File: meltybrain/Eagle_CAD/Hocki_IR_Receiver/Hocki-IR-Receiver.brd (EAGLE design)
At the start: 42 x 34 mm, 68 parts, among them J1 SM03B-SRSS-TB(LF)(SN), U1 OPA2380AIDGKR, U10 LMH6612MAX/NOPB, U11 LMH6612MAX/NOPB, U2 OPA2380AIDGKR, U3 TLV3502AIDCNR, U4 TLV3502AIDCNR, U5 SN74LVC1G58DCKR, U6 NL27WZ32USG, U7 TMUX1204DGSR, U8 AP2210K-5.0TRG1, U9 TLV73310PDBVT

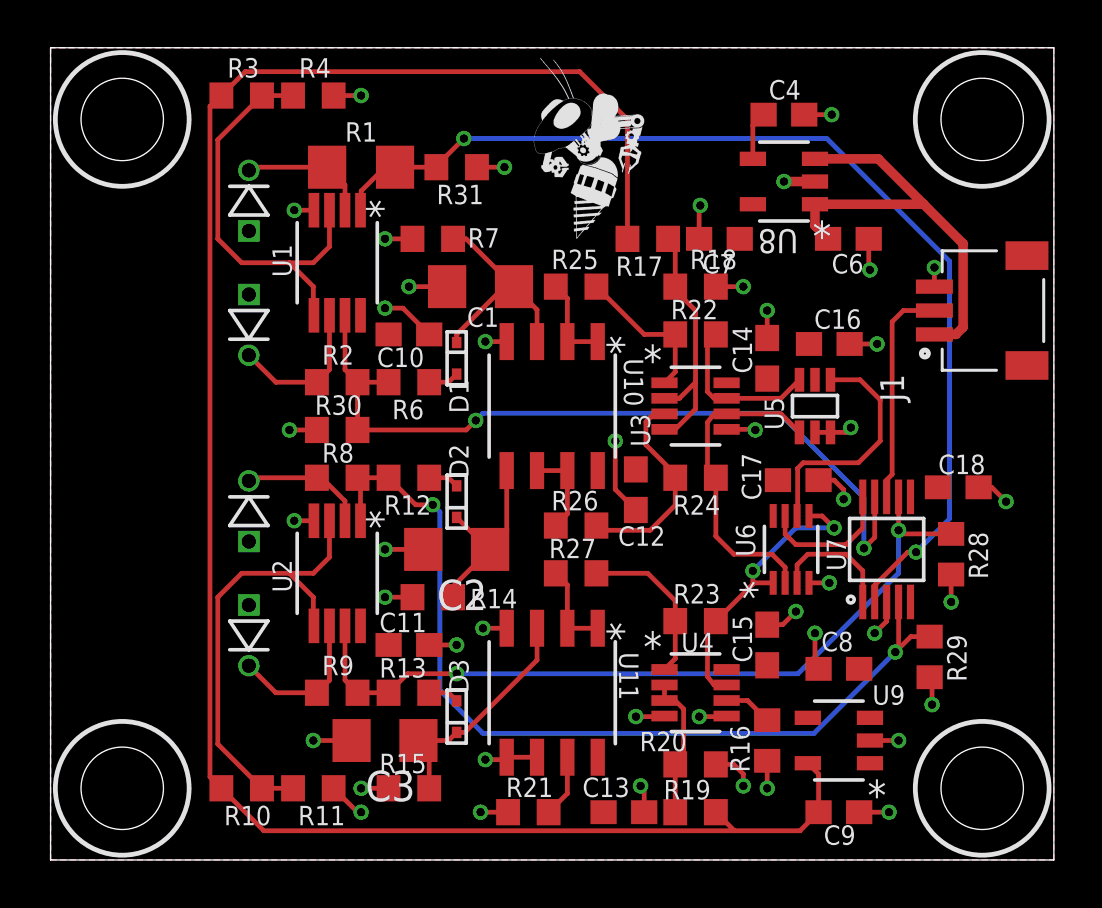
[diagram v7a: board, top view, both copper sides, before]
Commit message: power in
traces under capacitors be sketch...tried to avoid...
24-9 regulator is in
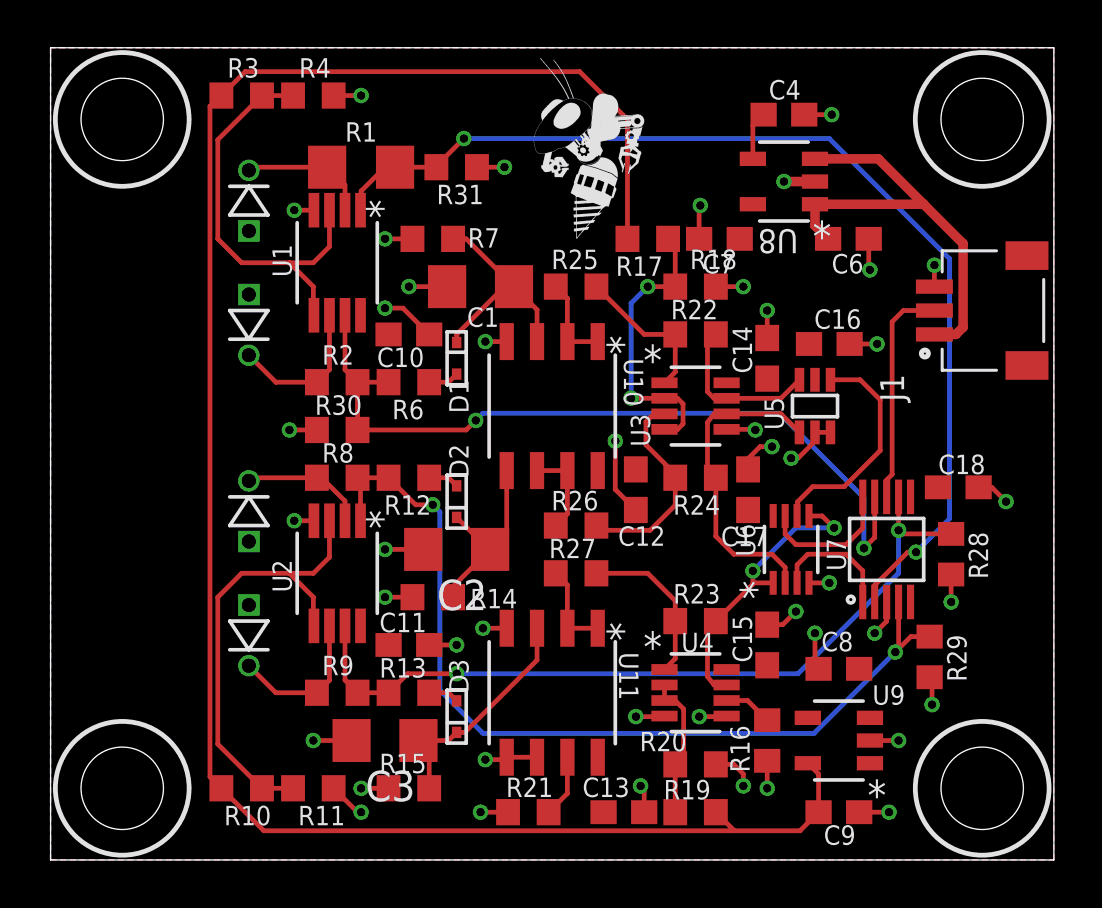
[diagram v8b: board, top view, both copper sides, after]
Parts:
- moved C17 2.14 mm to (29.2, 15.5), turned to 90 degrees
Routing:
- net N$13: track 10.8 -> 12.2 mm, vias 0 -> 2
- net GND: track 58.7 -> 59.6 mm
- net N$9: track 10.1 -> 9.50 mm
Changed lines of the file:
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@@
 <drawing>
 <settings>
-<setting alwaysvectorfont="no"/>
+<setting alwaysvectorfont="yes"/>
 <setting verticaltext="up"/>
 </settings>
@@
 <attribute name="VALUE" x="31.965" y="19.695" size="1.27" layer="27"/>
 </element>
-<element name="C17" library="rcl" library_urn="urn:adsk.eagle:library:334" package="C0603" package3d_urn="urn:adsk.eagle:package:23616/2" value="0.1u" x="31.3" y="15.9" smashed="yes">
-<attribute name="NAME" x="28.935" y="17.035" size="0.8128" layer="25" rot="R270"/>
-<attribute name="POPULARITY" value="37" x="31.3" y="15.9" size="1.778" layer="27" display="off"/>
-<attribute name="SPICEPREFIX" value="C" x="31.3" y="15.9" size="1.778" layer="27" display="off"/>
-<attribute name="VALUE" x="30.665" y="13.995" size="1.27" layer="27"/>
+<element name="C17" library="rcl" library_urn="urn:adsk.eagle:library:334" package="C0603" package3d_urn="urn:adsk.eagle:package:23616/2" value="0.1u" x="29.2" y="15.5" smashed="yes" rot="R90">
+<attribute name="NAME" x="28.065" y="13.135" size="0.8128" layer="25"/>
+<attribute name="POPULARITY" value="37" x="29.2" y="15.5" size="1.778" layer="27" rot="R90" display="off"/>
+<attribute name="SPICEPREFIX" value="C" x="29.2" y="15.5" size="1.778" layer="27" rot="R90" display="off"/>
+<attribute name="VALUE" x="31.105" y="14.865" size="1.27" layer="27" rot="R90"/>
 </element>
 <element name="C18" library="rcl" library_urn="urn:adsk.eagle:library:334" package="C0603" package3d_urn="urn:adsk.eagle:package:23616/2" value="0.1u" x="38" y="15.6" smashed="yes">
@@
 <wire x1="30" y1="4.15" x2="30" y2="3" width="0.2" layer="1"/>
 <via x="30" y="3" extent="1-16" drill="0.35"/>
-<wire x1="32" y1="17.9" x2="32.003790625" y2="17.896209375" width="0.2" layer="1"/>
-<wire x1="32.65" y1="17.9" x2="32.00758125" y2="17.9" width="0.2" layer="1"/>
-<wire x1="32.00758125" y1="17.9" x2="32.003790625" y2="17.896209375" width="0.2" layer="1"/>
 <wire x1="29" y1="3.1" x2="29" y2="3.6" width="0.2" layer="1"/>
 <wire x1="29" y1="3.6" x2="28.6" y2="4" width="0.2" layer="1"/>
@@
 <wire x1="34.6" y1="21.6" x2="33.45" y2="21.6" width="0.2" layer="1"/>
 <via x="34.6" y="21.6" extent="1-16" drill="0.35"/>
-<via x="33.2" y="15.1" extent="1-16" drill="0.35"/>
-<wire x1="32.15" y1="15.9" x2="32.8" y2="15.9" width="0.2" layer="1"/>
-<wire x1="33.2" y1="15.5" x2="33.2" y2="15.1" width="0.2" layer="1"/>
-<wire x1="33.2" y1="15.5" x2="32.8" y2="15.9" width="0.2" layer="1"/>
-<wire x1="32.65" y1="17.9" x2="33.3" y2="17.9" width="0.2" layer="1"/>
-<wire x1="33.3" y1="17.9" x2="33.5" y2="18.1" width="0.2" layer="1"/>
-<via x="33.5" y="18.1" extent="1-16" drill="0.35"/>
 <wire x1="35" y1="10.8" x2="35" y2="9.9936" width="0.2" layer="1"/>
 <wire x1="35" y1="9.9936" x2="34.5" y2="9.4936" width="0.2" layer="1"/>
@@
 <via x="30.7" y="28.4" extent="1-16" drill="0.35"/>
 <contactref element="J1" pad="3"/>
-<wire x1="37" y1="24" x2="37" y2="24.8" width="0.2" layer="1"/>
-<via x="37" y="24.8" extent="1-16" drill="0.35"/>
+<wire x1="37" y1="24" x2="37" y2="24.9" width="0.2" layer="1"/>
+<via x="37" y="24.9" extent="1-16" drill="0.35"/>
+<wire x1="29.2" y1="16.35" x2="29.2" y2="16.8" width="0.2" layer="1"/>
+<wire x1="29.7" y1="17.3" x2="30.2" y2="17.3" width="0.2" layer="1"/>
+<wire x1="29.7" y1="17.3" x2="29.2" y2="16.8" width="0.2" layer="1"/>
+<via x="30.2" y="17.3" extent="1-16" drill="0.35"/>
+<wire x1="32" y1="17.9" x2="32.65" y2="17.9" width="0.2" layer="1"/>
+<via x="31" y="16.8186" extent="1-16" drill="0.35"/>
+<wire x1="32" y1="17.9" x2="31.977" y2="17.877" width="0.2" layer="1"/>
+<wire x1="31.977" y1="17.877" x2="31.977" y2="17.505975" width="0.2" layer="1"/>
+<wire x1="31.977" y1="17.505975" x2="31.289625" y2="16.8186" width="0.2" layer="1"/>
+<wire x1="31.289625" y1="16.8186" x2="31" y2="16.8186" width="0.2" layer="1"/>
 </signal>
 <signal name="5V">
@@
 <via x="36.2306" y="12.88615" extent="1-16" drill="0.35"/>
 <wire x1="36.2306" y1="12.88615" x2="37.6306" y2="14.28615" width="0.2" layer="16"/>
-<wire x1="37.6306" y1="25.0694" x2="37.6306" y2="14.28615" width="0.2" layer="16"/>
-<wire x1="32.5" y1="30.2" x2="17.3" y2="30.2" width="0.2" layer="16"/>
+<wire x1="37.6306" y1="25.1694" x2="37.6306" y2="14.28615" width="0.2" layer="16"/>
+<wire x1="32.6" y1="30.2" x2="17.3" y2="30.2" width="0.2" layer="16"/>
 <via x="17.3" y="30.2" extent="1-16" drill="0.35"/>
 <wire x1="17.3" y1="30.2" x2="16.15" y2="29.05" width="0.2" layer="1"/>
 <wire x1="16.15" y1="29" x2="16.15" y2="29.05" width="0.2" layer="1"/>
 <wire x1="34.5" y1="11.5" x2="35.88615" y2="12.88615" width="0.2" layer="1"/>
-<wire x1="37.6306" y1="25.0694" x2="32.5" y2="30.2" width="0.2" layer="16"/>
+<wire x1="37.6306" y1="25.1694" x2="32.6" y2="30.2" width="0.2" layer="16"/>
 <contactref element="R31" pad="2"/>
 <contactref element="U1" pad="1"/>
@@
 <contactref element="U5" pad="4"/>
 <contactref element="U6" pad="6"/>
-<wire x1="34.7306" y1="19.26120625" x2="34.7306" y2="17.53879375" width="0.2" layer="1"/>
-<wire x1="31.505975" y1="16.627" x2="31.273" y2="16.394025" width="0.2" layer="1"/>
+<wire x1="34.7306" y1="19.26120625" x2="34.7306" y2="17.13879375" width="0.2" layer="1"/>
+<wire x1="31.905975" y1="15.627" x2="31.273" y2="14.994025" width="0.2" layer="1"/>
 <wire x1="31.273" y1="14.423" x2="31.25" y2="14.4" width="0.2" layer="1"/>
 <wire x1="34.7306" y1="19.26120625" x2="33.89180625" y2="20.1" width="0.2" layer="1"/>
 <wire x1="32.65" y1="20.1" x2="33.89180625" y2="20.1" width="0.2" layer="1"/>
-<wire x1="34.7306" y1="17.53879375" x2="33.81880625" y2="16.627" width="0.2" layer="1"/>
-<wire x1="33.81880625" y1="16.627" x2="31.505975" y2="16.627" width="0.2" layer="1"/>
-<wire x1="31.273" y1="16.394025" x2="31.273" y2="14.423" width="0.2" layer="1"/>
+<wire x1="34.7306" y1="17.13879375" x2="33.21880625" y2="15.627" width="0.2" layer="1"/>
+<wire x1="33.21880625" y1="15.627" x2="31.905975" y2="15.627" width="0.2" layer="1"/>
+<wire x1="31.273" y1="14.994025" x2="31.273" y2="14.423" width="0.2" layer="1"/>
 </signal>
 <signal name="A1">
@@
 <contactref element="U3" pad="2"/>
 <contactref element="U3" pad="4"/>
-<wire x1="26.15" y1="24" x2="26.15" y2="23.85" width="0.2" layer="1"/>
-<wire x1="26.15" y1="23.85" x2="27" y2="23" width="0.2" layer="1"/>
-<wire x1="27" y1="23" x2="27" y2="20" width="0.2" layer="1"/>
-<wire x1="27" y1="20" x2="26.325" y2="19.325" width="0.2" layer="1"/>
-<wire x1="26.325" y1="19.325" x2="25.7" y2="19.325" width="0.2" layer="1"/>
-<wire x1="27" y1="18.878975" x2="26.146025" y2="18.025" width="0.2" layer="1"/>
-<wire x1="26.146025" y1="18.025" x2="25.7" y2="18.025" width="0.2" layer="1"/>
-<wire x1="27" y1="20" x2="27" y2="18.878975" width="0.2" layer="1"/>
 <wire x1="26.15" y1="24" x2="26.15" y2="25.7" width="0.2" layer="1"/>
 <wire x1="26.15" y1="25.7" x2="25.85" y2="26" width="0.2" layer="1"/>
+<wire x1="26.15" y1="24" x2="25" y2="24" width="0.2" layer="1"/>
+<via x="25" y="24" extent="1-16" drill="0.35"/>
+<wire x1="25" y1="24" x2="24.3" y2="23.3" width="0.2" layer="16"/>
+<wire x1="24.3" y1="23.3" x2="24.3" y2="19.3306" width="0.2" layer="16"/>
+<via x="24.3" y="19.3306" extent="1-16" drill="0.35"/>
+<wire x1="24.3" y1="19.3306" x2="24.3056" y2="19.325" width="0.2" layer="1"/>
+<wire x1="24.3056" y1="19.325" x2="25.7" y2="19.325" width="0.2" layer="1"/>
+<wire x1="26.244025" y1="19.327" x2="26.477" y2="19.094025" width="0.2" layer="1"/>
+<wire x1="26.477" y1="19.094025" x2="26.477" y2="18.255975" width="0.2" layer="1"/>
+<wire x1="26.477" y1="18.255975" x2="26.244025" y2="18.023" width="0.2" layer="1"/>
+<wire x1="25.7" y1="19.325" x2="25.702" y2="19.327" width="0.2" layer="1"/>
+<wire x1="26.244025" y1="19.327" x2="25.702" y2="19.327" width="0.2" layer="1"/>
+<wire x1="26.244025" y1="18.023" x2="25.702" y2="18.023" width="0.2" layer="1"/>
+<wire x1="25.7" y1="18.025" x2="25.702" y2="18.023" width="0.2" layer="1"/>
 </signal>
 <signal name="N$14">
